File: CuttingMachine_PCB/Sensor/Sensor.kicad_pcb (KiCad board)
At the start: 2 copper layers, 20 x 25 mm, 4 parts, among them J1 Conn_01x03_Pin

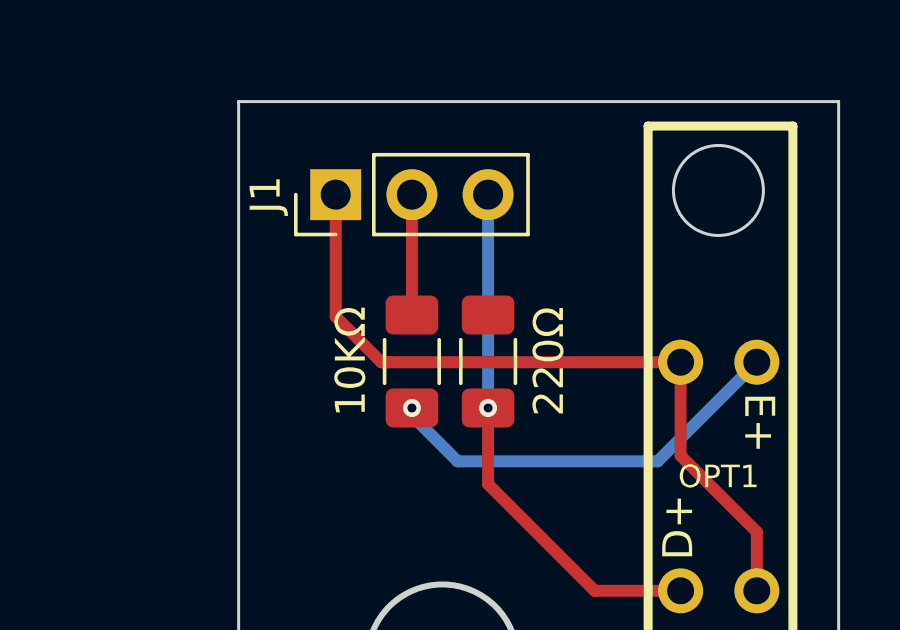
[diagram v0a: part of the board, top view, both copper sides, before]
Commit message: Fixed Error in Sensor board
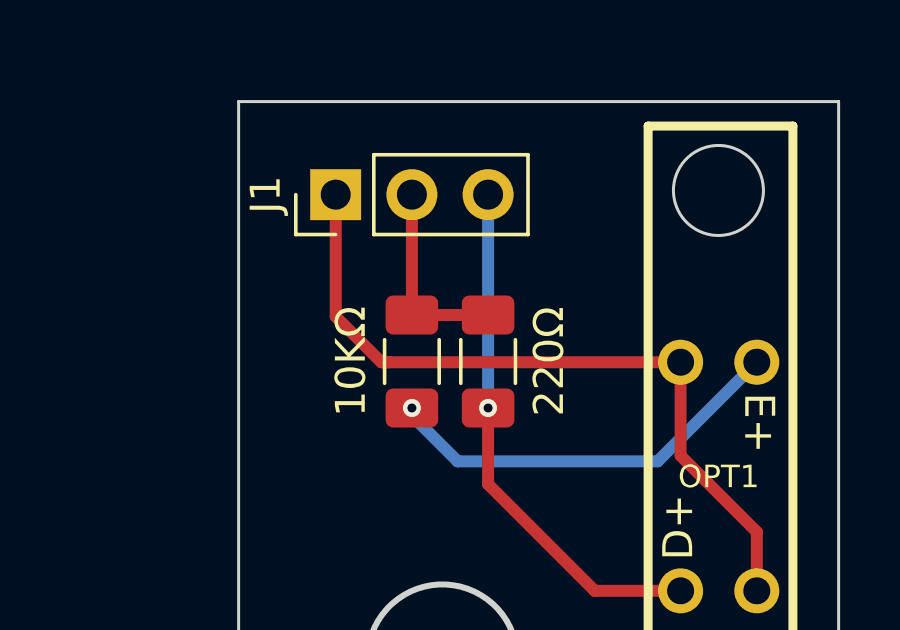
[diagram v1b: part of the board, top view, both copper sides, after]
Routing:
- net Net-(J1-Pin_2): track 4.01 -> 6.55 mm
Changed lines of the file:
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@@
 		)
 		(fp_text user "${REFERENCE}"
-			(at 0 2.54 360)
+			(at 0 2.54 0)
 			(layer "F.Fab")
 			(effects
@@
 		(width 0.4)
 		(layer "F.Cu")
+		(net 1)
+	)
+	(segment
+		(start 142.24 93.674)
+		(end 144.78 93.674)
+		(width 0.4)
+		(layer "F.Cu")

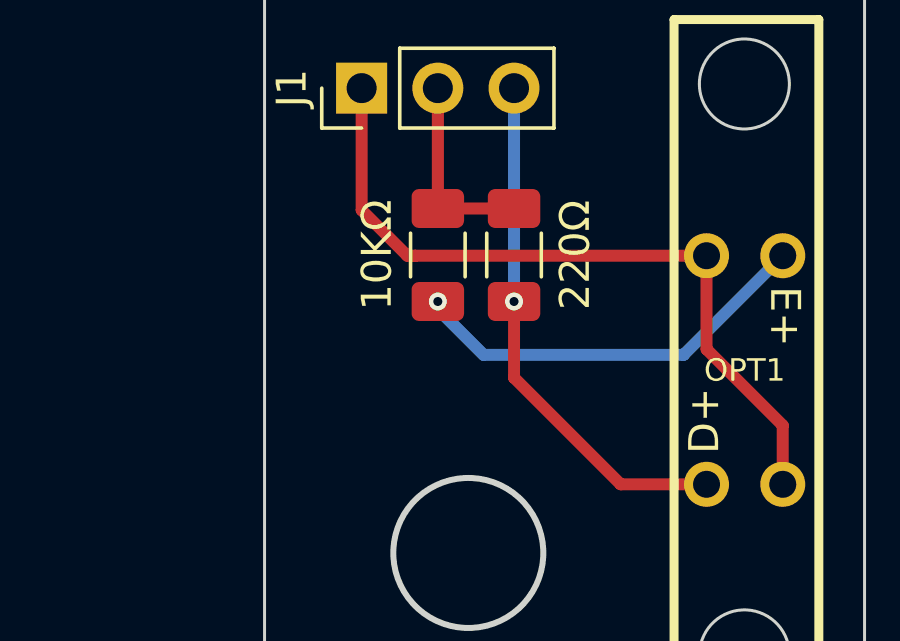
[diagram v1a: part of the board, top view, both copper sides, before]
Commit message: Revert "Update CuttingMachine_Firmware.ino"
This reverts commit 331047baca9097e741e2c189d087a95fc5961f25.
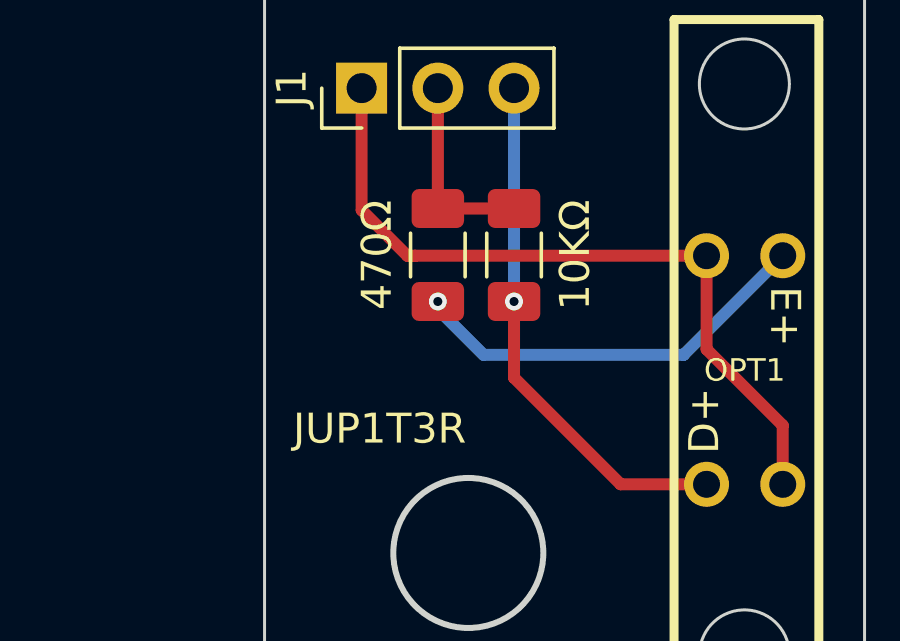
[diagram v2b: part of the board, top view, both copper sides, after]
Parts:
- renumbered 220Ω to 10KΩ, 10KΩ to 470Ω
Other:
- board text added: "JUP1T3R"
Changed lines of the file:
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@@
 		(descr "Resistor SMD 1206 (3216 Metric), square (rectangular) end terminal, IPC_7351 nominal with elongated pad for handsoldering. (Body size source: IPC-SM-782 page 72, https://www.pcb-3d.com/wordpress/wp-content/uploads/ipc-sm-782a_amendment_1_and_2.pdf), generated with kicad-footprint-generator")
 		(tags "resistor handsolder")
-		(property "Reference" "10KΩ"
+		(property "Reference" "470Ω"
 			(at 0 2.032 90)
 			(layer "F.SilkS")
@@
 		(descr "Resistor SMD 1206 (3216 Metric), square (rectangular) end terminal, IPC_7351 nominal with elongated pad for handsoldering. (Body size source: IPC-SM-782 page 72, https://www.pcb-3d.com/wordpress/wp-content/uploads/ipc-sm-782a_amendment_1_and_2.pdf), generated with kicad-footprint-generator")
 		(tags "resistor handsolder")
-		(property "Reference" "220Ω"
+		(property "Reference" "10KΩ"
 			(at 0 -2.032 90)
 			(layer "F.SilkS")
@@
 		)
 	)
+	(gr_text "JUP1T3R"
+		(at 137.414 101.6 0)
+		(layer "F.SilkS")
+		(effects
+			(font
+				(size 1 1)
+				(thickness 0.125)
+			)
+			(justify left bottom)
+		)
+	)
